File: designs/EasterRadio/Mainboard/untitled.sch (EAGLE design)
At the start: 52 parts, among them IC1 74HC595D, IC2 74HC595D, IC3 74HC595D, IC4 Analog Digital

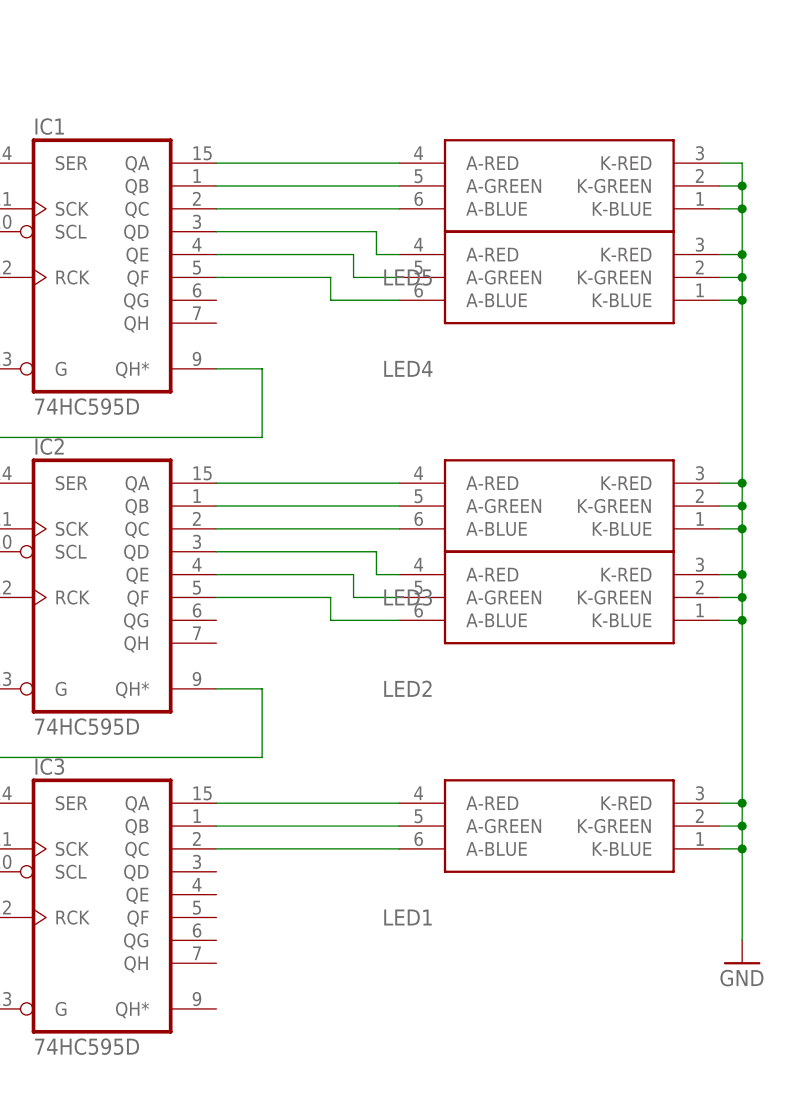
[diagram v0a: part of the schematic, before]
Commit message: changed mainboard design radio
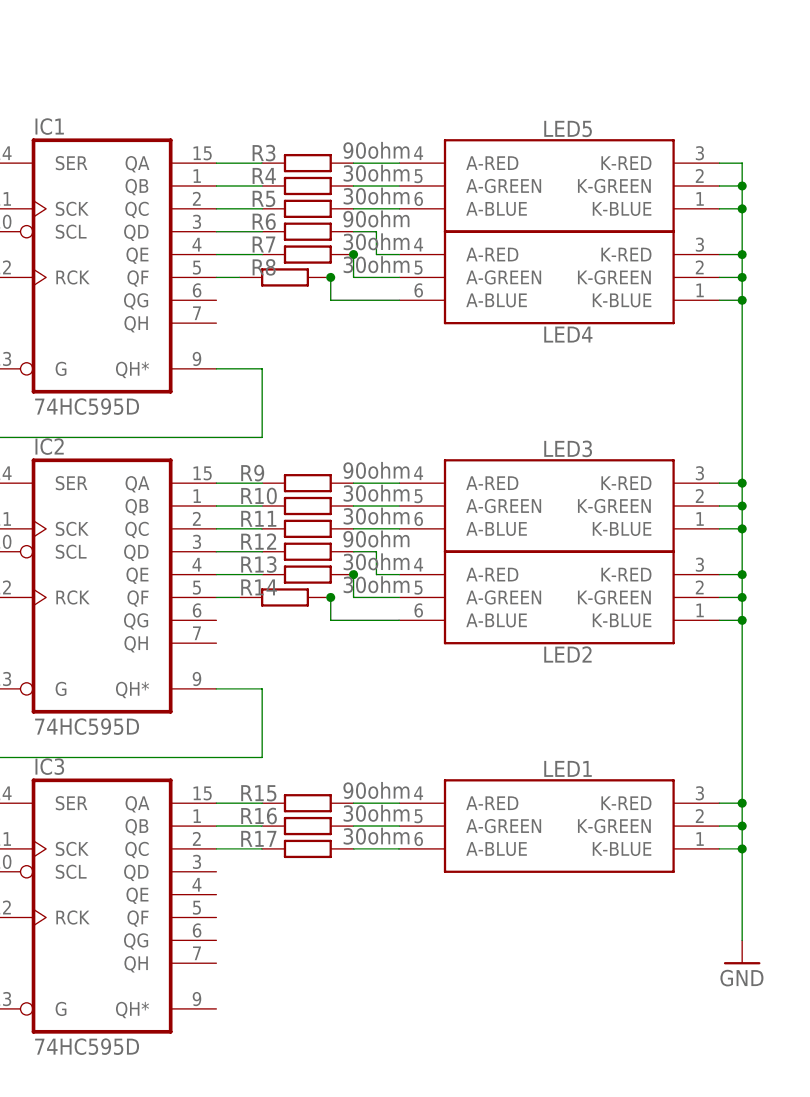
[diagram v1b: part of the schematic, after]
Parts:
- added R10, R11, R13, R14, R16, R17, R4, R5, R7, R8: 30ohm, rcl:R-EU_R0805
- added R12, R15, R3, R6, R9: 90ohm, rcl:R-EU_R0805
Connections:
- new net N$20: IC1A.QA, R3.1
- new net N$23: IC1A.QB, R4.1
- new net N$24: IC1A.QC, R5.1
- new net N$25: IC1A.QD, R6.1
- new net N$26: IC1A.QE, R7.1
- new net N$27: IC1A.QF, R8.1
- new net N$28: IC2A.QA, R9.1
- new net N$29: IC2A.QB, R10.1
- new net N$30: IC2A.QC, R11.1
- new net N$31: IC2A.QD, R12.1
- new net N$32: IC2A.QE, R13.1
- new net N$33: IC2A.QF, R14.1
- new net N$34: IC3A.QA, R15.1
- new net N$35: IC3A.QB, R16.1
- new net N$36: IC3A.QC, R17.1
- net N$10: now also R6.2; no longer IC1A.QD
- net N$11: now also R7.2; no longer IC1A.QE
- net N$12: now also R8.2; no longer IC1A.QF
- net N$13: now also R9.2; no longer IC2A.QA
- net N$14: now also R10.2; no longer IC2A.QB
- net N$15: now also R12.2; no longer IC2A.QD
- net N$16: now also R13.2; no longer IC2A.QE
- net N$18: now also R15.2; no longer IC3A.QA
- net N$19: now also R16.2; no longer IC3A.QB
- net N$3: now also R11.2; no longer IC2A.QC
- net N$4: now also R17.2; no longer IC3A.QC
- net N$6: now also R14.2; no longer IC2A.QF
- net N$7: now also R3.2; no longer IC1A.QA
- net N$8: now also R4.2; no longer IC1A.QB
- net N$9: now also R5.2; no longer IC1A.QC

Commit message: added new mainboard design
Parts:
- R1, R2: device rcl:R-EU_R0805 -> rcl:R-EU_R0603
- R10, R11, R12, R13, R14, R15, R16, R17, R3, R4, R5, R6, R7, R8, R9: device rcl:R-EU_R0805 -> rcl:R-EU_R0402
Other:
- moved on the sheet: R10, R11, R12, R13, R14, R15, R16, R17, R3, R4, R5, R6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

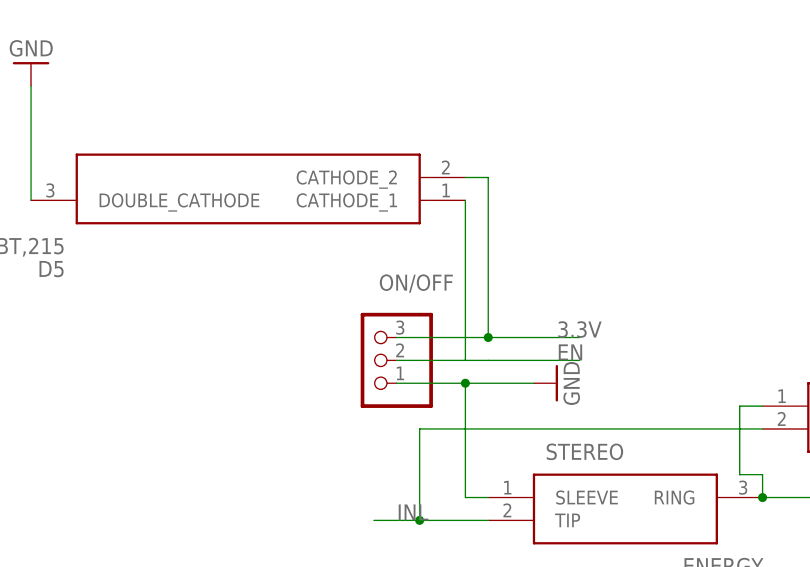
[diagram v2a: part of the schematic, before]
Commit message: added changes to mainboard for speaker
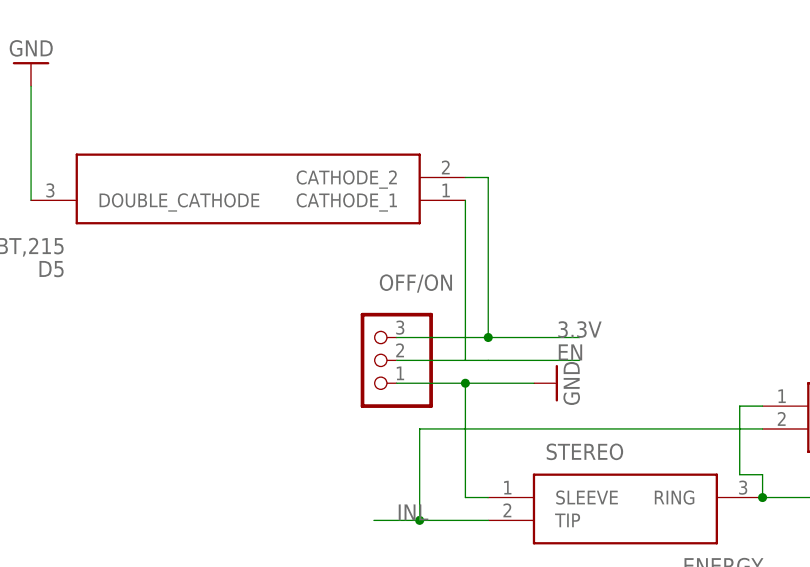
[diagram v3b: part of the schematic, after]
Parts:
- renumbered ON/OFF to OFF/ON
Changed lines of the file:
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@@
 <grid distance="0.1" unitdist="inch" unit="inch" style="lines" multiple="1" display="no" altdistance="0.01" altunitdist="inch" altunit="inch"/>
 <layers>
-<layer number="1" name="Top" color="4" fill="1" visible="yes" active="no"/>
-<layer number="2" name="Route2" color="16" fill="1" visible="yes" active="no"/>
-<layer number="3" name="Route3" color="17" fill="1" visible="yes" active="no"/>
-<layer number="4" name="Route4" color="18" fill="1" visible="yes" active="no"/>
-<layer number="5" name="Route5" color="19" fill="1" visible="yes" active="no"/>
-<layer number="6" name="Route6" color="25" fill="1" visible="yes" active="no"/>
-<layer number="7" name="Route7" color="26" fill="1" visible="yes" active="no"/>
-<layer number="8" name="Route8" color="27" fill="1" visible="yes" active="no"/>
-<layer number="9" name="Route9" color="28" fill="1" visible="yes" active="no"/>
-<layer number="10" name="Route10" color="29" fill="1" visible="yes" active="no"/>
-<layer number="11" name="Route11" color="30" fill="1" visible="yes" active="no"/>
-<layer number="12" name="Route12" color="20" fill="1" visible="yes" active="no"/>
-<layer number="13" name="Route13" color="21" fill="1" visible="yes" active="no"/>
-<layer number="14" name="Route14" color="22" fill="1" visible="yes" active="no"/>
-<layer number="15" name="Route15" color="23" fill="1" visible="yes" active="no"/>
-<layer number="16" name="Bottom" color="1" fill="1" visible="yes" active="no"/>
-<layer number="17" name="Pads" color="2" fill="1" visible="yes" active="no"/>
-<layer number="18" name="Vias" color="2" fill="1" visible="yes" active="no"/>
-<layer number="19" name="Unrouted" color="6" fill="1" visible="yes" active="no"/>
-<layer number="20" name="Dimension" color="24" fill="1" visible="yes" active="no"/>
-<layer number="21" name="tPlace" color="7" fill="1" visible="yes" active="no"/>
-<layer number="22" name="bPlace" color="7" fill="1" visible="yes" active="no"/>
-<layer number="23" name="tOrigins" color="15" fill="1" visible="yes" active="no"/>
-<layer number="24" name="bOrigins" color="15" fill="1" visible="yes" active="no"/>
-<layer number="25" name="tNames" color="7" fill="1" visible="yes" active="no"/>
-<layer number="26" name="bNames" color="7" fill="1" visible="yes" active="no"/>
-<layer number="27" name="tValues" color="7" fill="1" visible="yes" active="no"/>
-<layer number="28" name="bValues" color="7" fill="1" visible="yes" active="no"/>
+<layer number="1" name="Top" color="4" fill="1" visible="no" active="no"/>
+<layer number="2" name="Route2" color="16" fill="1" visible="no" active="no"/>
+<layer number="3" name="Route3" color="17" fill="1" visible="no" active="no"/>
+<layer number="4" name="Route4" color="18" fill="1" visible="no" active="no"/>
+<layer number="5" name="Route5" color="19" fill="1" visible="no" active="no"/>
+<layer number="6" name="Route6" color="25" fill="1" visible="no" active="no"/>
+<layer number="7" name="Route7" color="26" fill="1" visible="no" active="no"/>
+<layer number="8" name="Route8" color="27" fill="1" visible="no" active="no"/>
+<layer number="9" name="Route9" color="28" fill="1" visible="no" active="no"/>
+<layer number="10" name="Route10" color="29" fill="1" visible="no" active="no"/>
+<layer number="11" name="Route11" color="30" fill="1" visible="no" active="no"/>
+<layer number="12" name="Route12" color="20" fill="1" visible="no" active="no"/>
+<layer number="13" name="Route13" color="21" fill="1" visible="no" active="no"/>
+<layer number="14" name="Route14" color="22" fill="1" visible="no" active="no"/>
+<layer number="15" name="Route15" color="23" fill="1" visible="no" active="no"/>
+<layer number="16" name="Bottom" color="1" fill="1" visible="no" active="no"/>
+<layer number="17" name="Pads" color="2" fill="1" visible="no" active="no"/>
+<layer number="18" name="Vias" color="2" fill="1" visible="no" active="no"/>
+<layer number="19" name="Unrouted" color="6" fill="1" visible="no" active="no"/>
+<layer number="20" name="Dimension" color="24" fill="1" visible="no" active="no"/>
+<layer number="21" name="tPlace" color="7" fill="1" visible="no" active="no"/>
+<layer number="22" name="bPlace" color="7" fill="1" visible="no" active="no"/>
+<layer number="23" name="tOrigins" color="15" fill="1" visible="no" active="no"/>
+<layer number="24" name="bOrigins" color="15" fill="1" visible="no" active="no"/>
+<layer number="25" name="tNames" color="7" fill="1" visible="no" active="no"/>
+<layer number="26" name="bNames" color="7" fill="1" visible="no" active="no"/>
+<layer number="27" name="tValues" color="7" fill="1" visible="no" active="no"/>
+<layer number="28" name="bValues" color="7" fill="1" visible="no" active="no"/>
 <layer number="29" name="tStop" color="7" fill="3" visible="no" active="no"/>
 <layer number="30" name="bStop" color="7" fill="6" visible="no" active="no"/>
@@
 <layer number="35" name="tGlue" color="7" fill="4" visible="no" active="no"/>
 <layer number="36" name="bGlue" color="7" fill="5" visible="no" active="no"/>
-<layer number="37" name="tTest" color="7" fill="1" visible="yes" active="no"/>
-<layer number="38" name="bTest" color="7" fill="1" visible="yes" active="no"/>
+<layer number="37" name="tTest" color="7" fill="1" visible="no" active="no"/>
+<layer number="38" name="bTest" color="7" fill="1" visible="no" active="no"/>
 <layer number="39" name="tKeepout" color="4" fill="11" visible="no" active="no"/>
 <layer number="40" name="bKeepout" color="1" fill="11" visible="no" active="no"/>
@@
 <layer number="44" name="Drills" color="7" fill="1" visible="no" active="no"/>
 <layer number="45" name="Holes" color="7" fill="1" visible="no" active="no"/>
-<layer number="46" name="Milling" color="3" fill="1" visible="yes" active="no"/>
-<layer number="47" name="Measures" color="7" fill="1" visible="yes" active="no"/>
-<layer number="48" name="Document" color="7" fill="1" visible="yes" active="no"/>
-<layer number="49" name="Reference" color="7" fill="1" visible="yes" active="no"/>
-<layer number="50" name="dxf" color="7" fill="1" visible="yes" active="no"/>
-<layer number="51" name="tDocu" color="7" fill="1" visible="yes" active="no"/>
-<layer number="52" name="bDocu" color="7" fill="1" visible="yes" active="no"/>
-<layer number="53" name="tGND_GNDA" color="7" fill="1" visible="yes" active="no"/>
-<layer number="54" name="bGND_GNDA" color="7" fill="1" visible="yes" active="no"/>
-<layer number="56" name="wert" color="7" fill="1" visible="yes" active="no"/>
+<layer number="46" name="Milling" color="3" fill="1" visible="no" active="no"/>
+<layer number="47" name="Measures" color="7" fill="1" visible="no" active="no"/>
+<layer number="48" name="Document" color="7" fill="1" visible="no" active="no"/>
+<layer number="49" name="Reference" color="7" fill="1" visible="no" active="no"/>
+<layer number="50" name="dxf" color="7" fill="1" visible="no" active="no"/>
+<layer number="51" name="tDocu" color="7" fill="1" visible="no" active="no"/>
+<layer number="52" name="bDocu" color="7" fill="1" visible="no" active="no"/>
+<layer number="53" name="tGND_GNDA" color="7" fill="1" visible="no" active="no"/>
+<layer number="54" name="bGND_GNDA" color="7" fill="1" visible="no" active="no"/>
+<layer number="56" name="wert" color="7" fill="1" visible="no" active="no"/>
 <layer number="88" name="SimResults" color="9" fill="1" visible="yes" active="yes"/>
 <layer number="89" name="SimProbes" color="9" fill="1" visible="yes" active="yes"/>
@@
 <part name="IC2" library="NixieTube" deviceset="74*595" device="D" package3d_urn="urn:adsk.eagle:package:2010/1" technology="HC"/>
 <part name="IC3" library="NixieTube" deviceset="74*595" device="D" package3d_urn="urn:adsk.eagle:package:2010/1" technology="HC"/>
-<part name="ON/OFF" library="pinhead" library_urn="urn:adsk.eagle:library:325" deviceset="PINHD-1X3" device="" package3d_urn="urn:adsk.eagle:package:22458/2"/>
+<part name="OFF/ON" library="pinhead" library_urn="urn:adsk.eagle:library:325" deviceset="PINHD-1X3" device="" package3d_urn="urn:adsk.eagle:package:22458/2"/>
 <part name="GND1" library="supply1" library_urn="urn:adsk.eagle:library:371" deviceset="GND" device=""/>
 <part name="GND2" library="supply1" library_urn="urn:adsk.eagle:library:371" deviceset="GND" device=""/>
@@
 <attribute name="NAME" x="76.835" y="304.165" size="1.778" layer="95" rot="R90"/>
 </instance>
-<instance part="ON/OFF" gate="A" x="71.12" y="167.64" smashed="yes" rot="R180">
+<instance part="OFF/ON" gate="A" x="71.12" y="167.64" smashed="yes" rot="R180">
 <attribute name="NAME" x="80.01" y="177.165" size="1.778" layer="95" rot="R180"/>
 <attribute name="VALUE" x="77.47" y="175.26" size="1.778" layer="96" rot="R180"/>
@@
 <net name="3.3V" class="0">
 <segment>
-<pinref part="ON/OFF" gate="A" pin="3"/>
+<pinref part="OFF/ON" gate="A" pin="3"/>
 <label x="91.44" y="170.18" size="1.778" layer="95"/>
 <wire x1="73.66" y1="170.18" x2="83.82" y2="170.18" width="0.1524" layer="91"/>
@@
 <net name="EN" class="0">
 <segment>
-<pinref part="ON/OFF" gate="A" pin="2"/>
+<pinref part="OFF/ON" gate="A" pin="2"/>
 <label x="91.44" y="167.64" size="1.778" layer="95"/>
 <wire x1="73.66" y1="167.64" x2="81.28" y2="167.64" width="0.1524" layer="91"/>
@@
 <net name="GND" class="0">
 <segment>
-<pinref part="ON/OFF" gate="A" pin="1"/>
+<pinref part="OFF/ON" gate="A" pin="1"/>
 <wire x1="73.66" y1="165.1" x2="81.28" y2="165.1" width="0.1524" layer="91"/>
 <pinref part="GND1" gate="1" pin="GND"/>
